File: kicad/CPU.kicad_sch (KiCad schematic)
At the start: 13 parts, among them U3 68010P10, U4 GAL22V10, U5 SST39SF040, U6 AS6C4008-55PCN, U7 SST39SF040, U8 AS6C4008-55PCN

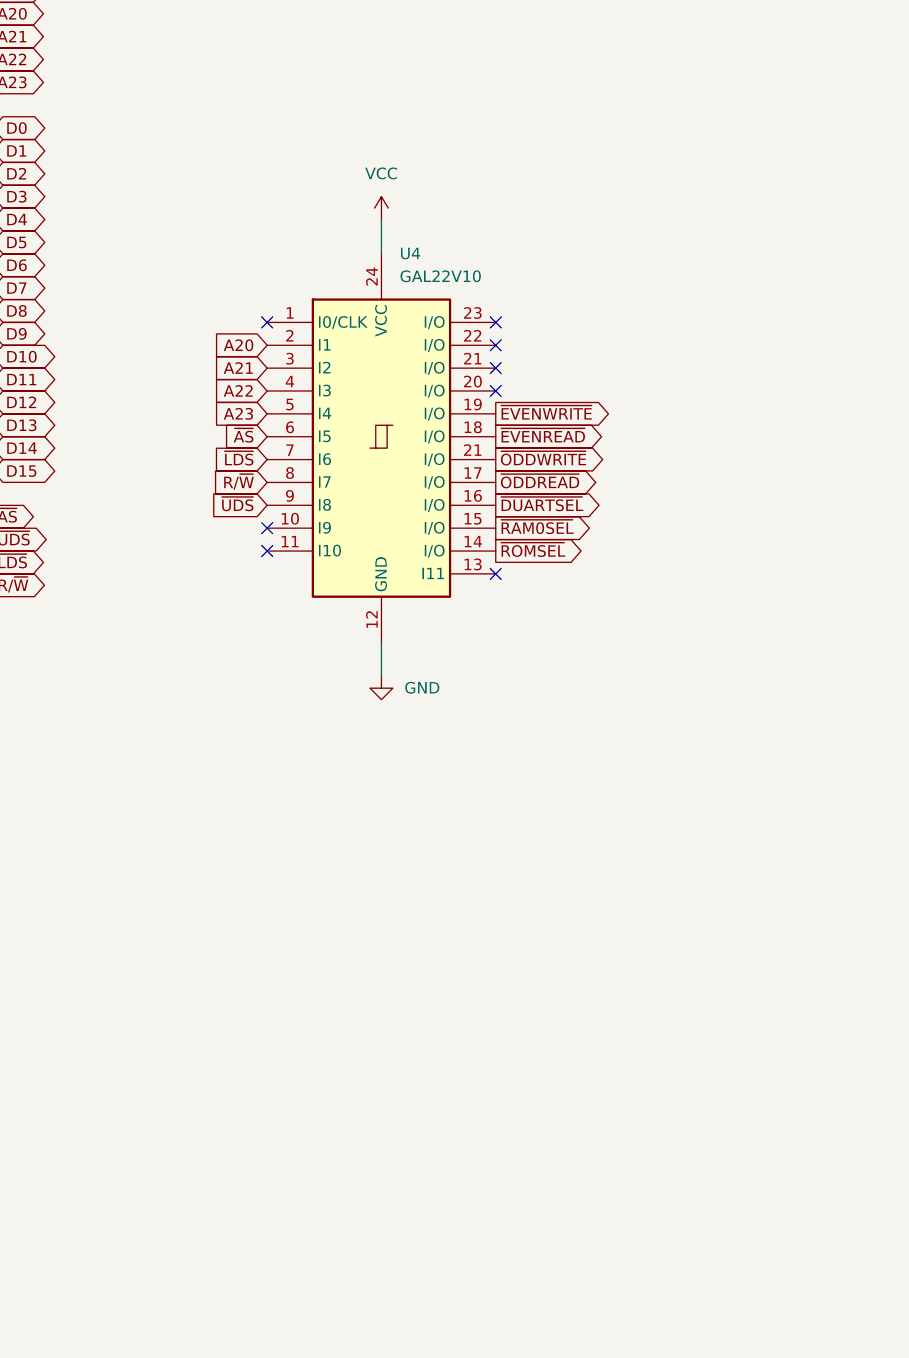
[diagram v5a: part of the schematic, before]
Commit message: Revamped gluelogic for IRQ and DTACK
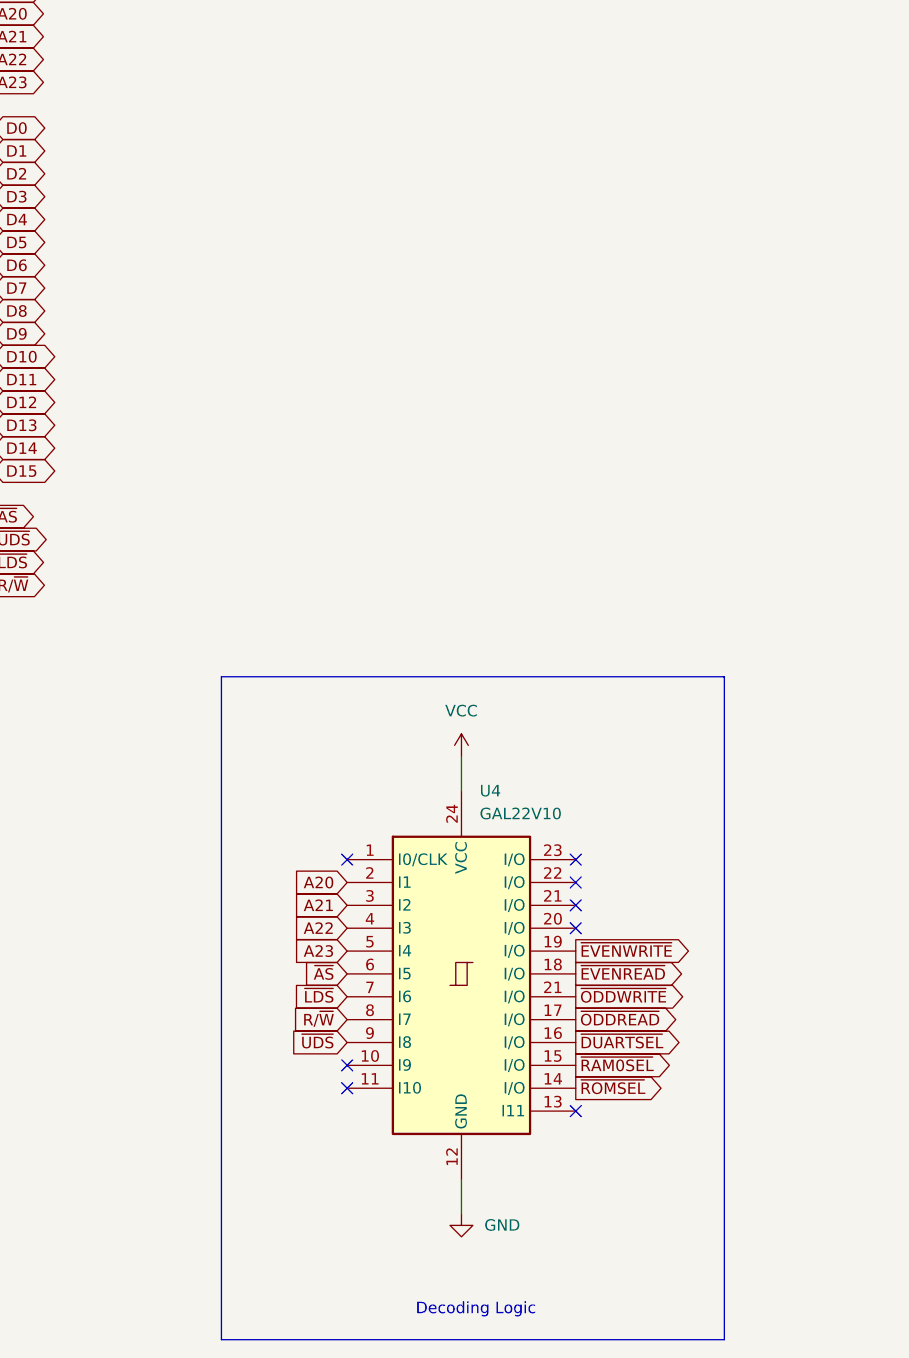
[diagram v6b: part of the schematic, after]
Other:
- note added: "Decoding Logic"
- moved on the sheet: U4

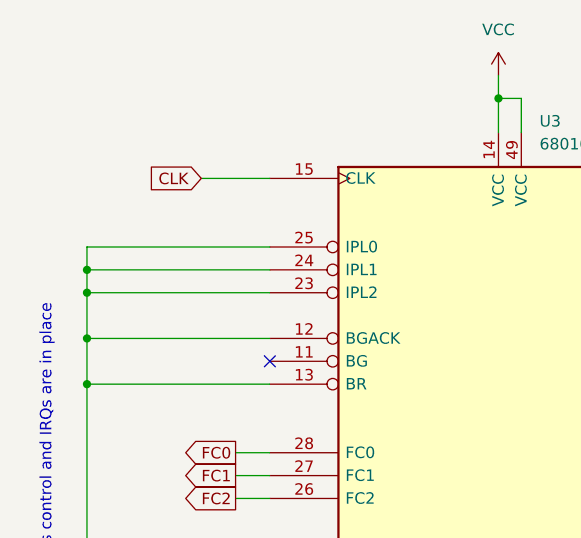
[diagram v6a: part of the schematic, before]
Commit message: - Added buffers for LED indicators in kicad - Removed pullups on FC0.2 in kicad - Connected FC0-2 to glue logic in kicad - Revamped glue logic for irg and iack in Digital
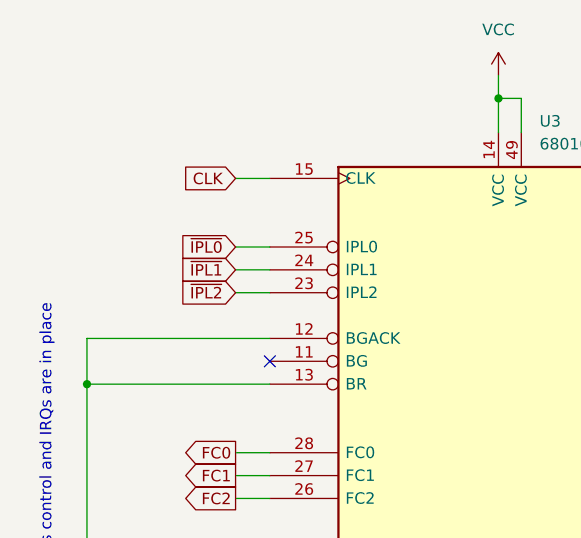
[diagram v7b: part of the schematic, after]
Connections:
- net at R8.2, U3.12 (BGACK), U3.13 (BR)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: no longer U3.23 (IPL2), U3.24 (IPL1), U3.25 (IPL0)
- new net ~{IPL0}: U3.25 (IPL0)
- new net ~{IPL1}: U3.24 (IPL1)
- new net ~{IPL2}: U3.23 (IPL2)
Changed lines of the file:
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@@
   (junction (at 160.02 59.69) (diameter 0) (color 0 0 0 0)
-  )
-  (junction (at 20.32 44.45) (diameter 0) (color 0 0 0 0)
-  )
-  (junction (at 20.32 41.91) (diameter 0) (color 0 0 0 0)
-  )
-  (junction (at 20.32 49.53) (diameter 0) (color 0 0 0 0)
   )
   (junction (at 172.72 59.69) (diameter 0) (color 0 0 0 0)
@@
     (stroke (width 0) (type default))
   )
-  (wire (pts (xy 40.64 41.91) (xy 20.32 41.91))
-    (stroke (width 0) (type default))
-  )
   (wire (pts (xy 172.72 59.69) (xy 185.42 59.69))
     (stroke (width 0) (type default))
@@
     (stroke (width 0) (type default))
   )
+  (wire (pts (xy 36.83 41.91) (xy 40.64 41.91))
+    (stroke (width 0) (type default))
+  )
   (wire (pts (xy 262.89 147.32) (xy 262.89 154.94))
     (stroke (width 0) (type default))
@@
     (stroke (width 0) (type default))
   )
-  (wire (pts (xy 40.64 44.45) (xy 20.32 44.45))
-    (stroke (width 0) (type default))
-  )
   (wire (pts (xy 20.32 49.53) (xy 40.64 49.53))
     (stroke (width 0) (type default))
   )
-  (wire (pts (xy 20.32 44.45) (xy 20.32 49.53))
-    (stroke (width 0) (type default))
-  )
-  (wire (pts (xy 20.32 39.37) (xy 20.32 41.91))
+  (wire (pts (xy 36.83 39.37) (xy 40.64 39.37))
     (stroke (width 0) (type default))
   )
@@
     (stroke (width 0) (type default))
   )
-  (wire (pts (xy 20.32 41.91) (xy 20.32 44.45))
-    (stroke (width 0) (type default))
-  )
   (wire (pts (xy 314.96 111.76) (xy 314.96 121.92))
     (stroke (width 0) (type default))
@@
     (stroke (width 0) (type default))
   )
-  (wire (pts (xy 33.02 31.75) (xy 40.64 31.75))
+  (wire (pts (xy 36.83 31.75) (xy 40.64 31.75))
     (stroke (width 0) (type default))
   )
@@
     (stroke (width 0) (type default))
   )
+  (wire (pts (xy 36.83 44.45) (xy 40.64 44.45))
+    (stroke (width 0) (type default))
+  )
   (wire (pts (xy 143.51 209.55) (xy 143.51 213.36))
     (stroke (width 0) (type default))
@@
   )
   (wire (pts (xy 20.32 88.9) (xy 20.32 90.17))
-    (stroke (width 0) (type default))
-  )
-  (wire (pts (xy 40.64 39.37) (xy 20.32 39.37))
     (stroke (width 0) (type default))
   )
@@
     )
   )
-  (global_label "CLK" (shape input) (at 33.02 31.75 180) (fields_autoplaced)
-    (effects (font (size 1.27 1.27)) (justify right))
-    (property "Intersheetrefs" "${INTERSHEET_REFS}" (at 27.0388 31.8294 0)
+  (global_label "CLK" (shape input) (at 36.83 31.75 180) (fields_autoplaced)
+    (effects (font (size 1.27 1.27)) (justify right))
+    (property "Intersheetrefs" "${INTERSHEET_REFS}" (at 30.8488 31.8294 0)
       (effects (font (size 1.27 1.27)) (justify right) hide)
     )
@@
     )
   )
+  (global_label "~{IPL0}" (shape input) (at 36.83 39.37 180) (fields_autoplaced)
+    (effects (font (size 1.27 1.27)) (justify right))
+    (property "Intersheetrefs" "${INTERSHEET_REFS}" (at 29.8118 39.37 0)
+      (effects (font (size 1.27 1.27)) (justify right) hide)
+    )
+  )
   (global_label "A18" (shape output) (at 91.44 74.93 0) (fields_autoplaced)
     (effects (font (size 1.27 1.27)) (justify left))
@@
     )
   )
+  (global_label "~{IPL2}" (shape input) (at 36.83 44.45 180) (fields_autoplaced)
+    (effects (font (size 1.27 1.27)) (justify right))
+    (property "Intersheetrefs" "${INTERSHEET_REFS}" (at 29.8118 44.45 0)
+      (effects (font (size 1.27 1.27)) (justify right) hide)
+    )
+  )
   (global_label "A17" (shape input) (at 299.72 91.44 180) (fields_autoplaced)
     (effects (font (size 1.27 1.27)) (justify right))
@@
       (effects (font (size 1.27 1.27)) (justify right) hide)
     )
+  )
+  (global_label "~{IPL1}" (shape input) (at 36.83 41.91 180) (fields_autoplaced)
+    (effects (font (size 1.27 1.27)) (justify right))
+    (property "Intersheetrefs" "${INTERSHEET_REFS}" (at 29.8118 41.91 0)
+      (effects (font (size 1.27 1.27)) (justify right) hide)
+    )
